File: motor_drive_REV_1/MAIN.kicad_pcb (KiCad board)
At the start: 2 copper layers, 115 parts, among them J1 Conn_01x04, J2 Conn_01x02, J3 Conn_01x04, J4 Conn_01x06, J5 Conn_01x06, J6 Conn_01x02, J7 Conn_01x02, Q1 nmos, Q2 nmos, Q3 nmos, Q4 nmos, Q5 nmos, Q6 nmos, U1 AD8418ABRMZ-RL, U2 AD8418ABRMZ-RL, U3 AD8418ABRMZ-RL, U4 AD8418ABRMZ-RL, U5 ADA4571WHRZ-R7, U6 SN65LBC176QDRQ1, U7 FAN7888_gen, U8 TMS20F28027PTT-custom, U9 AD8418ABRMZ-RL

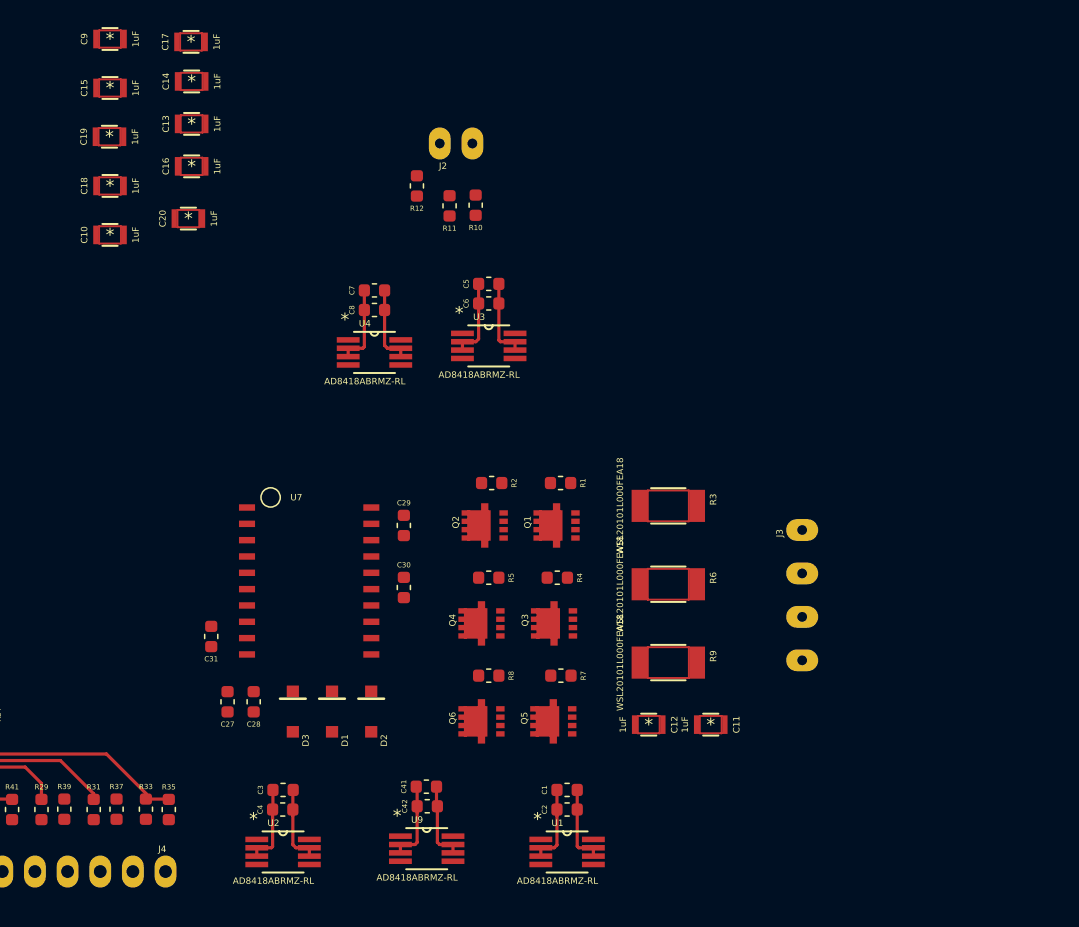
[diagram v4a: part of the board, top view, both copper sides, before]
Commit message: gate drive rework and schematic re-organization
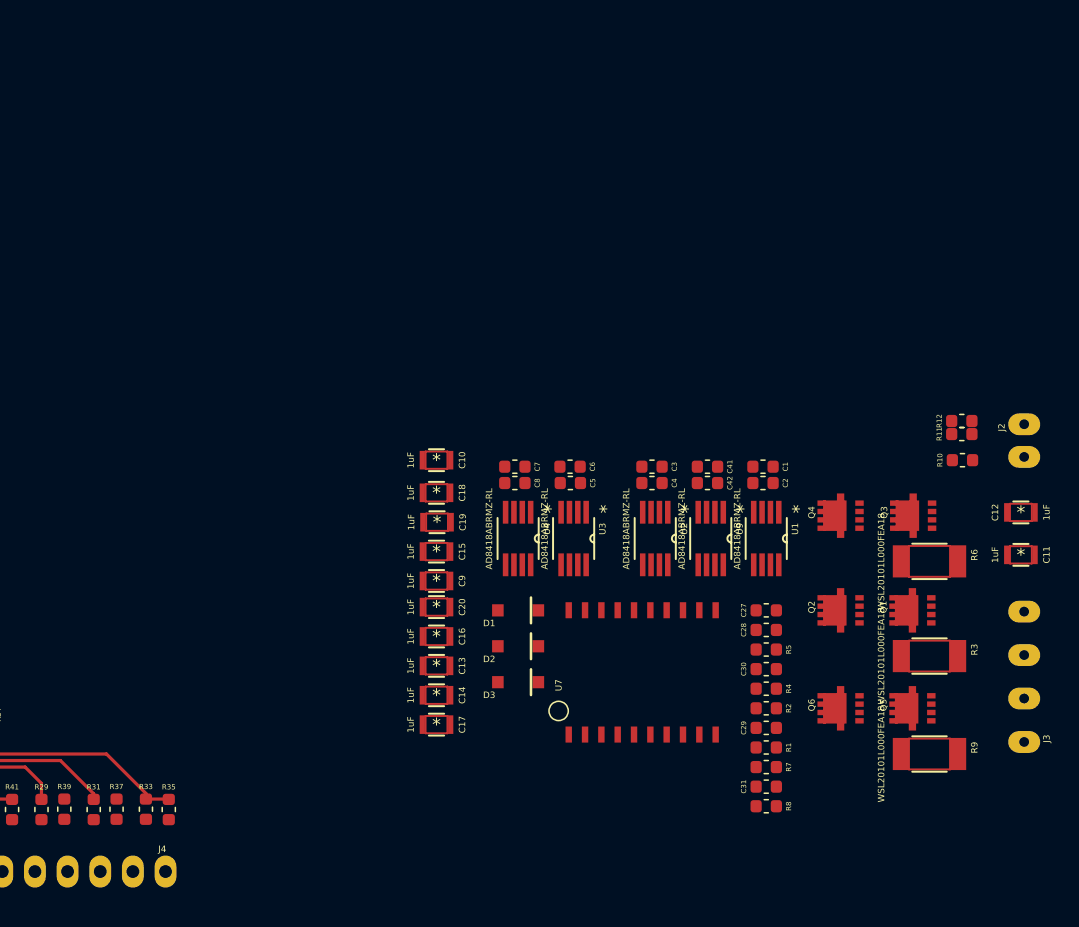
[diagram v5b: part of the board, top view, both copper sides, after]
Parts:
- moved C17 56.4 mm to (158.5, 111.8), turned to 180 degrees
- moved C14 51.4 mm to (158.5, 109.5), turned to 180 degrees
- moved J2 50.4 mm to (204.2, 88.4), turned to 270 degrees
- moved C9 49.2 mm to (158.5, 100.6), turned to 180 degrees
- moved C13 46.3 mm to (158.5, 107.2), turned to 180 degrees
- moved R12 46.2 mm to (199.4, 88.1), turned to 0 degrees
- moved C31 44.7 mm to (184.2, 116.6), turned to 0 degrees
- moved C15 44.1 mm to (158.5, 98.3), turned to 180 degrees
- moved R11 43.6 mm to (199.4, 89.2), turned to 0 degrees
- moved R10 42.8 mm to (199.4, 91.2), turned to 0 degrees
- moved C27 42.5 mm to (184.2, 102.9), turned to 0 degrees
- moved C16 41.2 mm to (158.5, 104.9), turned to 180 degrees
- moved C28 40.3 mm to (184.2, 104.4), turned to 0 degrees
- moved C19 39.4 mm to (158.5, 96.0), turned to 180 degrees
- moved C4 38.3 mm to (175.3, 93.0), turned to 180 degrees
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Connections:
- C10 pad 1: /DC_Link_Input/5.0V -> /DC_pos
- C10 pad 2: /DC_Link_Input/GND -> /DC_neg
- C13 pad 1: /DC_Link_Input/5.0V -> /DC_pos
- C13 pad 2: /DC_Link_Input/GND -> /DC_neg
- C14 pad 1: /DC_Link_Input/5.0V -> /DC_pos
- C14 pad 2: /DC_Link_Input/GND -> /DC_neg
- C15 pad 1: /DC_Link_Input/5.0V -> /DC_pos
- C15 pad 2: /DC_Link_Input/GND -> /DC_neg
- C16 pad 1: /DC_Link_Input/5.0V -> /DC_pos
- C16 pad 2: /DC_Link_Input/GND -> /DC_neg
- C17 pad 1: /DC_Link_Input/5.0V -> /DC_pos
- C17 pad 2: /DC_Link_Input/GND -> /DC_neg
- C18 pad 1: /DC_Link_Input/5.0V -> /DC_pos
- C18 pad 2: /DC_Link_Input/GND -> /DC_neg
- C19 pad 1: /DC_Link_Input/5.0V -> /DC_pos
- C19 pad 2: /DC_Link_Input/GND -> /DC_neg
- C20 pad 1: /DC_Link_Input/5.0V -> /DC_pos
- C20 pad 2: /DC_Link_Input/GND -> /DC_neg
- C9 pad 1: /DC_Link_Input/5.0V -> /DC_pos
- C9 pad 2: /DC_Link_Input/GND -> /DC_neg
- J3 pad 1: /I_sense_n1 -> /half_bridge_1/M
- J3 pad 2: /I_sense_n2 -> /half_bridge_2/M
- J3 pad 3: /I_sense_n3 -> /half_bridge_3/M
- R3 pad 1: /I_sense_n1 -> /half_bridge_1/M
- R6 pad 1: /I_sense_n2 -> /half_bridge_2/M
- R9 pad 1: /I_sense_n3 -> /half_bridge_3/M
- U1 pad 1: /I_sense_n2 -> /DC_neg
- U2 pad 1: /I_sense_n3 -> /DC_neg
- U4 pad 1: /DC_neg -> (no net)
- U9 pad 1: /I_sense_n1 -> /DC_neg
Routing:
- net /GND: track 79.9 -> 48.3 mm
- net /5.0V: track 67.0 -> 35.4 mm

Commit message: second try at layout
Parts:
- removed U9: AD8418ABRMZ-RL, motor_drive_footprints:AD8418ABRMZ-RL
- added C45: 0.01uF, motor_drive_footprints:C_0603_1608Metric, F.Cu at (130.9, 88.5)
- added C46: C, motor_drive_footprints:C_0603_1608Metric, F.Cu at (156.6, 104.8)
- added C47: C, motor_drive_footprints:C_0603_1608Metric, F.Cu at (156.6, 109.8)
- added D4: LED, motor_drive_footprints:C_0603_1608Metric, F.Cu at (128.5, 121.8)
- added D5: LED, motor_drive_footprints:C_0603_1608Metric, F.Cu at (132.5, 114.8)
- added D6: LED, motor_drive_footprints:C_0603_1608Metric, F.Cu at (124.5, 124.3)
- added R45: 10, motor_drive_footprints:C_0603_1608Metric, F.Cu at (142.9, 87.4)
- added R46: 10, motor_drive_footprints:C_0603_1608Metric, F.Cu at (133.4, 96.0)
- added R47: 10, motor_drive_footprints:C_0603_1608Metric, F.Cu at (138.9, 90.5)
- added R48: 10, motor_drive_footprints:C_0603_1608Metric, F.Cu at (134.9, 93.5)
- added R49: WSL20101L000FEA18, motor_drive_footprints:WSL20101L000FEA18, F.Cu at (122.9, 83.7)
- added R50: WSL20101L000FEA18, motor_drive_footprints:WSL20101L000FEA18, F.Cu at (127.9, 77.0)
- added R51: R, motor_drive_footprints:C_0603_1608Metric, F.Cu at (156.6, 107.3)
- added R52: R, motor_drive_footprints:C_0603_1608Metric, F.Cu at (160.6, 104.8)
- added SW1: EVQ-Q2B01W, motor_drive_footprints:EVQ-Q2B01W, F.Cu at (108.7, 122.3)
- added SW2: EVQ-Q2B01W, motor_drive_footprints:EVQ-Q2B01W, F.Cu at (108.7, 114.4)
- C1, C7: value 1uF -> 2.2uF
- C10, C9: value 1uF -> 0.01uF; footprint motor_drive_footprints:gen_0805 -> motor_drive_footprints:C_0603_1608Metric
- C11, C14: value 1uF -> 4.7uF; footprint motor_drive_footprints:gen_0805 -> motor_drive_footprints:C_0603_1608Metric
- C12, C15: footprint motor_drive_footprints:gen_0805 -> motor_drive_footprints:C_0603_1608Metric
- C13: value 1uF -> 100pF; footprint motor_drive_footprints:gen_0805 -> motor_drive_footprints:C_0603_1608Metric
- C21, C23, C27, C32: value 2.2uF -> 1uF; footprint motor_drive_footprints:C_0603_1608Metric -> motor_drive_footprints:gen_0805
- C22, C24, C28: value 0.01uF -> 1uF; footprint motor_drive_footprints:C_0603_1608Metric -> motor_drive_footprints:gen_0805
- C25, C26: value 680pF -> 1uF; footprint motor_drive_footprints:C_0603_1608Metric -> motor_drive_footprints:gen_0805
- C29, C30, C31: value 0.22uF -> 1uF; footprint motor_drive_footprints:C_0603_1608Metric -> motor_drive_footprints:gen_0805
- C3: value 1uF -> 680pF
- C33: value 2.2uF -> C
- C34, C35: value 0.01uF -> C
- C36, C39: value 4.7uF -> C
- C37, C40, C41: value 1uF -> C
- C38: value 100pF -> C
- C4: value 0.01uF -> 680pF
- C42: value 0.01uF -> 1uF
- C43: value C -> 1uF
- C44: value C -> 0.01uF
- C5: value 1uF -> 0.01uF
- C6, C8: value 0.01uF -> 2.2uF
- D1, D2, D3: value D -> LED; footprint motor_drive_footprints:SOD123 -> motor_drive_footprints:C_0603_1608Metric
- J2: value Conn_01x02 -> Conn_01x06; footprint motor_drive_footprints:2pos_254 -> motor_drive_footprints:6pos_254
- J3: value Conn_01x04 -> Conn_01x06; footprint motor_drive_footprints:4pos_338 -> motor_drive_footprints:6pos_254
- J4: value Conn_01x06 -> Conn_01x03; footprint motor_drive_footprints:6pos_254 -> motor_drive_footprints:3pos_254
- J5: value Conn_01x06 -> Conn_01x04; footprint motor_drive_footprints:6pos_254 -> motor_drive_footprints:4pos_338
- R1, R2, R7, R8: value 10 -> 375
- R10: value R -> 4.7k
- R11, R12, R23: value R -> 10k
- R13: value NP -> 10k
- R14, R24: value 4.7k -> 10k
- R15, R16, R17, R25: value 375 -> 10k
- R18: value 680 -> 10k
- R19: value 120 -> 4.7k
- R20: value 680 -> 4.7k
- R22: value 375 -> 2.2k
- R26: value 2.2k -> 10k
- R3: value WSL20101L000FEA18 -> 680; footprint motor_drive_footprints:WSL20101L000FEA18 -> motor_drive_footprints:C_0603_1608Metric
- R31, R32, R33, R34: value 10k -> 375
- R39, R40, R41, R42: value 375 -> R
- R4: value 10 -> 120
- R43, R44: value R -> 10
- R5: value 10 -> 680
- R6: value WSL20101L000FEA18 -> 375; footprint motor_drive_footprints:WSL20101L000FEA18 -> motor_drive_footprints:C_0603_1608Metric
- R9: value WSL20101L000FEA18 -> NP; footprint motor_drive_footprints:WSL20101L000FEA18 -> motor_drive_footprints:C_0603_1608Metric
- U1: value AD8418ABRMZ-RL -> ADA4571WHRZ-R7
- U2: value AD8418ABRMZ-RL -> SN65LBC176QDRQ1; footprint motor_drive_footprints:AD8418ABRMZ-RL -> motor_drive_footprints:SN65LBC176QDRQ1
- U3: value AD8418ABRMZ-RL -> TMS20F28027PTT-custom; footprint motor_drive_footprints:AD8418ABRMZ-RL -> motor_drive_footprints:TMS320F28027PTT
- U4: value AD8418ABRMZ-RL -> TPS28225DR; footprint motor_drive_footprints:AD8418ABRMZ-RL -> motor_drive_footprints:TPS28225DR
- U5: value ADA4571WHRZ-R7 -> TPS28225DR; footprint motor_drive_footprints:AD8418ABRMZ-RL -> motor_drive_footprints:TPS28225DR
- U6: value SN65LBC176QDRQ1 -> TPS28225DR; footprint motor_drive_footprints:SN65LBC176QDRQ1 -> motor_drive_footprints:TPS28225DR
- U7: value FAN7888_gen -> AD8418ABRMZ-RL; footprint motor_drive_footprints:FAN7888 -> motor_drive_footprints:AD8418ABRMZ-RL
- U8: value TMS20F28027PTT-custom -> AD8418ABRMZ-RL; footprint motor_drive_footprints:TMS320F28027PTT -> motor_drive_footprints:AD8418ABRMZ-RL
- moved J2 102.1 mm to (104.2, 108.7), turned to 0 degrees
- moved J3 100.3 mm to (104.2, 105.2), turned to 0 degrees
- moved C12 88.4 mm to (120.5, 124.3)
- moved R11 87.4 mm to (116.5, 116.8)
- moved Q3 82.0 mm to (113.6, 92.3), turned to 0 degrees
- moved R12 79.6 mm to (128.5, 124.3)
- moved J1 78.4 mm to (152.5, 76.7)
- moved Q2 77.6 mm to (112.6, 96.9), turned to 0 degrees
- moved Q6 74.1 mm to (118.1, 92.3), turned to 0 degrees
- moved C11 73.0 mm to (132.3, 112.3), turned to 0 degrees
- moved Q5 72.8 mm to (128.8, 81.4), turned to 0 degrees
- moved U7 69.2 mm to (106.6, 94.2)
- moved Q1 66.8 mm to (133.8, 77.2), turned to 0 degrees
- moved C29 64.8 mm to (121.2, 96.6)
- moved C31 61.9 mm to (126.7, 93.5)
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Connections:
- C1 pad 1: /GND -> /5.0V
- C1 pad 2: /5.0V -> /GND
- C10 pad 1: /DC_pos -> /5.0V
- C10 pad 2: /DC_neg -> /GND
- C11 pad 1: /DC_pos -> /5.0V
- C11 pad 2: /phase_shield -> /GND
- C12 pad 1: /phase_shield -> Net-(C12-Pad1)
- C12 pad 2: /DC_neg -> /GND
- C13 pad 1: /DC_pos -> /GND
- C13 pad 2: /DC_neg -> /chip_reset
- C14 pad 1: /DC_pos -> Net-(C14-Pad1)
- C14 pad 2: /DC_neg -> /GND
- C15 pad 1: /DC_pos -> /5.0V
- C15 pad 2: /DC_neg -> /GND
- C16 pad 1: /DC_pos -> /power/DC_pos
- C16 pad 2: /DC_neg -> /power/DC_neg
- C17 pad 1: /DC_pos -> /power/DC_pos
- C17 pad 2: /DC_neg -> /power/DC_neg
- C18 pad 1: /DC_pos -> /power/DC_pos
- C18 pad 2: /DC_neg -> /power/DC_neg
- C19 pad 1: /DC_pos -> /power/DC_pos
- C19 pad 2: /DC_neg -> /power/shield
- C2 pad 1: /GND -> /5.0V
- C2 pad 2: /5.0V -> /GND
- C20 pad 1: /DC_pos -> /power/shield
- C20 pad 2: /DC_neg -> /power/DC_neg
- C21 pad 1: /5.0V -> /power/DC_pos
- C21 pad 2: /GND -> /power/DC_neg
- C22 pad 1: /5.0V -> /power/DC_pos
- C22 pad 2: /GND -> /power/DC_neg
- C23 pad 1: /5.0V -> /power/DC_pos
- C23 pad 2: /GND -> /power/DC_neg
- C24 pad 1: /5.0V -> /power/DC_pos
- C24 pad 2: /GND -> /power/DC_neg
- C25 pad 1: Net-(C25-Pad1) -> /power/DC_pos
- C25 pad 2: /5.0V -> /power/DC_neg
- C26 pad 1: /GND -> /power/DC_pos
- C26 pad 2: Net-(C26-Pad2) -> /power/DC_neg
- C27 pad 1: /5.0V -> /power/DC_pos
- C27 pad 2: /GND -> /power/DC_neg
- C28 pad 1: /5.0V -> /power/DC_pos
- C28 pad 2: /GND -> /power/DC_neg
- C29 pad 1: Net-(C29-Pad1) -> /power/DC_pos
- C29 pad 2: /I_sense_p1 -> /power/DC_neg
- C3 pad 2: /5.0V -> Net-(C3-Pad2)
- C30 pad 1: Net-(C30-Pad1) -> /power/DC_pos
- C30 pad 2: /I_sense_p2 -> /power/DC_neg
- C31 pad 1: Net-(C31-Pad1) -> /power/DC_pos
- C31 pad 2: /I_sense_p3 -> /power/DC_neg
- C32 pad 1: /5.0V -> /power/DC_pos
- C32 pad 2: /GND -> /power/DC_neg
- C33 pad 1: /5.0V -> /GND
- C33 pad 2: /GND -> /7.5V
- C34 pad 1: /5.0V -> /GND
- C34 pad 2: /GND -> /7.5V
- C35 pad 1: /5.0V -> /GND
- C35 pad 2: /GND -> /7.5V
- C36 pad 1: /5.0V -> Net-(C36-Pad1)
- C36 pad 2: /GND -> /power/SW_0
- C37 pad 2: /GND -> /power/SW_1
- C38 pad 1: /GND -> Net-(C38-Pad1)
- C38 pad 2: /chip_reset -> /power/SW_2
- C39 pad 1: Net-(C39-Pad1) -> /GND
- C39 pad 2: /GND -> /7.5V
- C4 pad 1: /GND -> Net-(C4-Pad1)
- C40 pad 1: /5.0V -> /GND
- C40 pad 2: /GND -> /7.5V
- C41 pad 2: /5.0V -> /7.5V
- C42 pad 2: /5.0V -> /7.5V
- C43 pad 1: /therm_1 -> /GND
- C43 pad 2: /GND -> /7.5V
- C44 pad 1: /therm_2 -> /GND
- C44 pad 2: /GND -> /7.5V
- C7 pad 1: /GND -> /5.0V
- C7 pad 2: /5.0V -> /GND
- C8 pad 1: /GND -> /5.0V
- C8 pad 2: /5.0V -> /GND
- C9 pad 1: /DC_pos -> /5.0V
- C9 pad 2: /DC_neg -> /GND
- D1 pad 1: Net-(C29-Pad1) -> Net-(D1-Pad1)
- D2 pad 1: Net-(C30-Pad1) -> Net-(D2-Pad1)
- D3 pad 1: Net-(C31-Pad1) -> Net-(D3-Pad1)
- J1 pad 2: /balance -> /RS422/balance
- J1 pad 3: /B -> /RS422/B
- J1 pad 4: /A -> /RS422/A
- J2 pad 1: /DC_neg -> /MOSI
- J2 pad 2: /IDC_sense_p -> /MISO
- J3 pad 1: /half_bridge_1/M -> /F28027/JTAG_TCK
- J3 pad 2: /half_bridge_2/M -> /F28027/JTAG_TDO
- J3 pad 3: /half_bridge_3/M -> /F28027/JTAG_TMS
- J3 pad 4: /phase_shield -> /F28027/JTAG_TDI
- J4 pad 1: /MOSI -> /power/DC_pos
- J4 pad 2: /MISO -> /power/DC_neg
- J4 pad 3: /nEN -> /power/shield
- J5 pad 1: /F28027/JTAG_TCK -> /power/U
- J5 pad 2: /F28027/JTAG_TDO -> /power/V
- J5 pad 3: /F28027/JTAG_TMS -> /power/SW_2
- J5 pad 4: /F28027/JTAG_TDI -> /power/shield
- J6 pad 2: /therm_1 -> /therm_0
- J7 pad 2: /therm_2 -> /therm_1
- L1 pad 1: Net-(C37-Pad1) -> Net-(C12-Pad1)
- L2 pad 2: Net-(C39-Pad1) -> Net-(C14-Pad1)
- Q1 pad 1: /DC_pos -> /power/DC_pos
- Q1 pad 3: /I_sense_p1 -> /power/SW_0
- Q2 pad 1: /I_sense_p1 -> /power/SW_0
- Q2 pad 3: /DC_neg -> /power/DC_neg
- Q3 pad 1: /DC_pos -> /power/DC_pos
- Q3 pad 3: /I_sense_p2 -> /power/SW_1
- Q4 pad 1: /I_sense_p2 -> /power/SW_1
- Q4 pad 3: /DC_neg -> /power/DC_neg
- Q5 pad 1: /DC_pos -> /power/DC_pos
- Q5 pad 3: /I_sense_p3 -> /power/SW_2
- Q6 pad 1: /I_sense_p3 -> /power/SW_2
- Q6 pad 3: /DC_neg -> /power/DC_neg
- R1 pad 1: Net-(Q1-Pad2) -> Net-(C3-Pad2)
- R1 pad 2: /GH_1 -> /RS422/A
- R10 pad 1: /DC_pos -> /DEnRE
- R10 pad 2: /IDC_sense_p -> /GND
- R11 pad 1: /DC_pos -> /5.0V
- R11 pad 2: /VDC_sense_p -> /F28027/BUTTON_0
- R12 pad 1: /VDC_sense_p -> /5.0V
- R12 pad 2: /DC_neg -> /F28027/BUTTON_1
- R13 pad 1: /5.0V -> Net-(D1-Pad1)
- R13 pad 2: /DEnRE -> /F28027/LED_0
- R14 pad 1: /DEnRE -> Net-(D2-Pad1)
- R14 pad 2: /GND -> /F28027/LED_1
- R15 pad 1: /UART_RX -> Net-(D3-Pad1)
- R15 pad 2: Net-(R15-Pad2) -> /F28027/LED_2
- R16 pad 1: /UART_TX -> Net-(D4-Pad1)
- R16 pad 2: Net-(R16-Pad2) -> /F28027/LED_3
- R17 pad 1: /GND -> Net-(D5-Pad1)
- R17 pad 2: /balance -> /F28027/LED_4
- R18 pad 1: Net-(C25-Pad1) -> Net-(D6-Pad1)
- R18 pad 2: /5.0V -> /F28027/LED_5
- R19 pad 1: Net-(C25-Pad1) -> /GND
- R19 pad 2: Net-(C26-Pad2) -> Net-(R19-Pad2)
- R2 pad 1: Net-(Q2-Pad2) -> Net-(C4-Pad1)
- R2 pad 2: /GL_1 -> /RS422/B
- R20 pad 2: Net-(C26-Pad2) -> Net-(R20-Pad2)
- R21 pad 1: Net-(C25-Pad1) -> Net-(R19-Pad2)
- R21 pad 2: /B -> /F28027/JTAG_nTRST
- R22 pad 1: Net-(C26-Pad2) -> /chip_reset
- R22 pad 2: /A -> /5.0V
- R23 pad 1: /GND -> Net-(R23-Pad1)
- R23 pad 2: Net-(R23-Pad2) -> /5.0V
- R24 pad 1: /GND -> Net-(R24-Pad1)
- R24 pad 2: Net-(R24-Pad2) -> /5.0V
- R25 pad 1: Net-(R23-Pad2) -> Net-(R25-Pad1)
- R25 pad 2: /F28027/JTAG_nTRST -> /5.0V
- R26 pad 1: /chip_reset -> Net-(R26-Pad1)
- R3 pad 1: /half_bridge_1/M -> /GND
- R3 pad 2: /I_sense_p1 -> Net-(C3-Pad2)
- R31 pad 1: Net-(R31-Pad1) -> Net-(R29-Pad1)
- R31 pad 2: /5.0V -> /MOSI
- R32 pad 1: Net-(R32-Pad1) -> Net-(R30-Pad1)
- R32 pad 2: /5.0V -> /F28027/JTAG_TCK
- R33 pad 1: Net-(R33-Pad1) -> Net-(R27-Pad1)
- R33 pad 2: /5.0V -> /MISO
- R34 pad 1: Net-(R34-Pad1) -> Net-(R28-Pad1)
- R34 pad 2: /5.0V -> /F28027/JTAG_TDO
- R35 pad 1: Net-(R33-Pad1) -> Net-(R25-Pad1)
- R35 pad 2: /MOSI -> /CLK
- R36 pad 1: Net-(R34-Pad1) -> Net-(R26-Pad1)
- R36 pad 2: /F28027/JTAG_TCK -> /F28027/JTAG_TMS
- R37 pad 1: Net-(R31-Pad1) -> Net-(R23-Pad1)
- R37 pad 2: /MISO -> /nEN
- R38 pad 1: Net-(R32-Pad1) -> Net-(R24-Pad1)
- R38 pad 2: /F28027/JTAG_TDO -> /F28027/JTAG_TDI
- R39 pad 1: Net-(R29-Pad1) -> /power/DC_neg
- R39 pad 2: /CLK -> /GND
- R4 pad 1: Net-(Q3-Pad2) -> Net-(C4-Pad1)
- R4 pad 2: /GH_2 -> Net-(C3-Pad2)
- R40 pad 1: Net-(R30-Pad1) -> Net-(R40-Pad1)
- R40 pad 2: /F28027/JTAG_TMS -> /7.5V
- R41 pad 1: Net-(R27-Pad1) -> Net-(R41-Pad1)
- R41 pad 2: /nEN -> /7.5V
- R42 pad 1: Net-(R28-Pad1) -> Net-(R42-Pad1)
- R42 pad 2: /F28027/JTAG_TDI -> /7.5V
- R43 pad 1: /therm_1 -> Net-(Q1-Pad2)
- R43 pad 2: /GND -> /power/GH_0
- R44 pad 1: /therm_2 -> Net-(Q2-Pad2)
- R44 pad 2: /GND -> /power/GL_0
- R5 pad 1: Net-(Q4-Pad2) -> Net-(C4-Pad1)
- R5 pad 2: /GL_2 -> /5.0V
- R6 pad 1: /half_bridge_2/M -> /GND
- R6 pad 2: /I_sense_p2 -> /RS422/balance
- R7 pad 1: Net-(Q5-Pad2) -> /UART_TX
- R7 pad 2: /GH_3 -> Net-(R7-Pad2)
- R8 pad 1: Net-(Q6-Pad2) -> /UART_RX
- R8 pad 2: /GL_3 -> Net-(R8-Pad2)
- R9 pad 1: /half_bridge_3/M -> /5.0V
- R9 pad 2: /I_sense_p3 -> /DEnRE
- U1 pad 1: /DC_neg -> /GND
- U1 pad 2: /GND -> /cos
- U1 pad 4: (no net) -> /sin
- U1 pad 5: /I_sense_2 -> (no net)
- U1 pad 6: /5.0V -> /GND
- U1 pad 8: /I_sense_p2 -> /GND
- U2 pad 1: /DC_neg -> Net-(R8-Pad2)
- U2 pad 2: /GND -> /DEnRE
- U2 pad 3: /GND -> /DEnRE
- U2 pad 4: (no net) -> Net-(R7-Pad2)
- U2 pad 5: /I_sense_3 -> /GND
- U2 pad 6: /5.0V -> Net-(C3-Pad2)
- U2 pad 7: /5.0V -> Net-(C4-Pad1)
- U2 pad 8: /I_sense_p3 -> /5.0V
- U3 pad 1: /DC_pos -> /UART_TX
- U3 pad 2: /GND -> Net-(R19-Pad2)
- U3 pad 3: /GND -> /chip_reset
- U3 pad 4: (no net) -> /I_sense_1
- U3 pad 5: /IDC_sense -> /I_sense_2
- U3 pad 6: /5.0V -> /sin
- U3 pad 7: /5.0V -> /cos
- U3 pad 8: /IDC_sense_p -> (no net)
- U4 pad 1: (no net) -> /power/GH_0
- U4 pad 2: /GND -> Net-(C36-Pad1)
- U4 pad 3: /GND -> (no net)
- U4 pad 4: (no net) -> /GND
- U4 pad 5: /VDC_sense -> /power/GL_0
- U4 pad 6: /5.0V -> /7.5V
- U4 pad 7: /5.0V -> Net-(R40-Pad1)
- U4 pad 8: /VDC_sense_p -> /power/SW_0
- U5 pad 1: /GND -> /power/GH_1
- U5 pad 2: /cos -> Net-(C37-Pad1)
- U5 pad 3: /GND -> (no net)
- U5 pad 4: /sin -> /GND
- U5 pad 5: (no net) -> /power/GL_1
- U5 pad 6: /GND -> /7.5V
- U5 pad 7: /5.0V -> Net-(R41-Pad1)
- U5 pad 8: /GND -> /power/SW_1
- U6 pad 1: Net-(R15-Pad2) -> /power/GH_2
- U6 pad 2: /DEnRE -> Net-(C38-Pad1)
- U6 pad 3: /DEnRE -> (no net)
- U6 pad 4: Net-(R16-Pad2) -> /GND
- U6 pad 5: /GND -> /power/GL_2
- U6 pad 6: Net-(C26-Pad2) -> /7.5V
- U6 pad 7: Net-(C25-Pad1) -> Net-(R42-Pad1)
- U6 pad 8: /5.0V -> /power/SW_2
- U7 pad 1: /HS_1 -> /power/SW_0
- U7 pad 2: /LS_1 -> /GND
- U7 pad 3: /HS_2 -> /GND
- U7 pad 4: /LS_2 -> (no net)
- U7 pad 5: /HS_3 -> (no net)
- U7 pad 6: /LS_3 -> /7.5V
- U7 pad 7: /GL_3 -> /7.5V
- U7 pad 8: /I_sense_p3 -> /power/U
- U8 pad 1: /UART_TX -> /power/SW_1
- U8 pad 2: Net-(R23-Pad2) -> /GND
- U8 pad 3: /chip_reset -> /GND
- U8 pad 4: /I_sense_1 -> (no net)
- U8 pad 5: /I_sense_2 -> /I_sense_1
- U8 pad 6: /I_sense_3 -> /7.5V
- U8 pad 7: /IDC_sense -> /7.5V
- U8 pad 8: /VDC_sense -> /power/V
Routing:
- net /GND: track 48.3 -> 0.00 mm, vias 3 -> 0
- net /5.0V: track 35.4 -> 0.00 mm, vias 7 -> 0
- net Net-(R33-Pad1): track 24.5 -> 0.00 mm
- net Net-(R31-Pad1): track 18.4 -> 0.00 mm
- net Net-(R29-Pad1): track 14.5 -> 0.00 mm
- net Net-(R28-Pad1): track 13.7 -> 0.00 mm
- net Net-(R27-Pad1): track 12.3 -> 0.00 mm
- net Net-(R30-Pad1): track 10.2 -> 0.00 mm
- net Net-(C25-Pad1): track 9.58 -> 0.00 mm
- net Net-(C26-Pad2): track 9.39 -> 0.00 mm
- net Net-(R32-Pad1): track 8.66 -> 0.00 mm
- net Net-(R34-Pad1): track 8.50 -> 0.00 mm
- net /DEnRE: track 7.47 -> 0.00 mm
- net Net-(C39-Pad1): track 6.36 -> 0.00 mm
- net /F28027/JTAG_TDI: track 6.23 -> 0.00 mm
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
